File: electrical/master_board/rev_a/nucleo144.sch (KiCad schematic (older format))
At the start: 1 part, among them CN95 NUCLEO-F767ZI;2xF2x35

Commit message: Switched from x166 to x165 shift registers.  Add bin/spi_sim.py.
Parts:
- added Q25: 2N7000;SOT23, Package_TO_SOT_SMD:SOT-23, symbol Transistor_FET:2N7000
- added R68: 100KΩ;1608, Resistor_SMD:R_0603_1608Metric, symbol Device:R_US
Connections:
- net labels added: 3.3V, DIO_SS
- wire segments 108 -> 120
- no-connect marks 58 -> 56
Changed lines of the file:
@@
 Wire Wire Line
 	10000 4700 10000 4800
-Text HLabel 8100 5950 0    50   Input ~ 0
+Text HLabel 6700 6000 0    50   Input ~ 0
 GND
 Wire Wire Line
-	8100 5950 10000 5950
-Wire Wire Line
-	10000 5950 10000 5700
+	6700 6000 7100 6000
+Wire Wire Line
+	10000 6000 10000 5700
 Connection ~ 10000 5700
 NoConn ~ 8400 4800
@@
 Text HLabel 3500 2900 2    50   Output ~ 0
 RMOTOR_CTL2
-Text HLabel 7000 4700 2    50   Input ~ 0
+Text HLabel 4600 7200 2    50   Input ~ 0
 ~MOTOR_FAULT_IN
 Text HLabel 6000 2000 2    50   Input ~ 0
@@
 DIO_MISO
 Wire Wire Line
-	5500 3200 6000 3200
+	5500 3200 5700 3200
 Wire Wire Line
 	6000 3300 5500 3300
@@
 Wire Wire Line
 	6000 1000 5500 1000
-Text HLabel 7000 4800 2    50   Output ~ 0
+Text HLabel 4600 7300 2    50   Output ~ 0
 ~MOTOR_FAULT_OUT
 Wire Wire Line
-	7000 4700 6900 4700
-Wire Wire Line
-	6900 4700 6900 4800
-Wire Wire Line
-	6900 4800 7000 4800
+	4600 7200 4500 7200
+Wire Wire Line
+	4500 7200 4500 7300
+Wire Wire Line
+	4500 7300 4600 7300
 Wire Wire Line
 	5500 1400 6000 1400
-Text HLabel 7000 4500 2    50   Input ~ 0
+Text HLabel 4600 7000 2    50   Input ~ 0
 ~ESTOP_IN
 Text HLabel 6000 1500 2    50   Input ~ 0
@@
 Text Notes 8850 4350 0    50   ~ 0
 Morpho Power Pins.
-Text HLabel 7000 4600 2    50   Output ~ 0
+Text HLabel 4600 7100 2    50   Output ~ 0
 ~MOTOR_SLEEP
 Wire Wire Line
-	7000 4500 6900 4500
-Wire Wire Line
-	6900 4500 6900 4600
-Wire Wire Line
-	6900 4600 7000 4600
+	4600 7000 4500 7000
+Wire Wire Line
+	4500 7000 4500 7100
+Wire Wire Line
+	4500 7100 4600 7100
 Wire Wire Line
 	5500 1500 6000 1500
@@
 Wire Wire Line
 	5500 800  6000 800
-Text Notes 6900 4400 0    50   ~ 0
+Text Notes 4500 6900 0    50   ~ 0
 Cross Sheet Connetions
 Text HLabel 3500 5000 2    50   Input ~ 0
@@
 Text HLabel 6000 5600 2    50   Input ~ 0
 SERVO_POS
-NoConn ~ 7000 5000
-NoConn ~ 7000 5100
 Wire Wire Line
 	5500 1100 6000 1100
 Wire Wire Line
 	5500 5600 6000 5600
+$Comp
+L Transistor_FET:2N7000 Q?
+U 1 1 5FC61D2B
+P 7000 5400
+AR Path="/5F79BC00/5FC61D2B" Ref="Q?"  Part="1"
+AR Path="/5FA4A874/5FC61D2B" Ref="Q?"  Part="1"
+AR Path="/5FAD82EE/5FC61D2B" Ref="Q?"  Part="1"
+AR Path="/5F8C2F57/5FC61D2B" Ref="Q?"  Part="1"
+AR Path="/5F3221A2/5FC61D2B" Ref="Q25"  Part="1"
+F 0 "Q25" H 6900 5550 50  0000 L CNN
+F 1 "2N7000;SOT23" H 7150 5250 50  0000 L CNN
+F 2 "Package_TO_SOT_SMD:SOT-23" H 7200 5325 50  0001 L CIN
+F 3 "https://www.fairchildsemi.com/datasheets/2N/2N7000.pdf" H 7000 5400 50  0001 L CNN
+	1    7000 5400
+	1    0    0    -1
+$EndComp
+Wire Wire Line
+	5700 3200 5700 4400
+Wire Wire Line
+	5700 4400 6200 4400
+Wire Wire Line
+	6200 4400 6200 5400
+Wire Wire Line
+	6200 5400 6800 5400
+Connection ~ 5700 3200
+Wire Wire Line
+	5700 3200 6000 3200
+Connection ~ 7100 6000
+Wire Wire Line
+	7100 6000 10000 6000
+$Comp
+L Device:R_US R?
+U 1 1 5FC830FC
+P 7100 4850
+AR Path="/5F52F39E/5FC830FC" Ref="R?"  Part="1"
+AR Path="/5F3221A2/5FC830FC" Ref="R68"  Part="1"
+F 0 "R68" H 6950 4950 50  0000 L CNN
+F 1 "100KΩ;1608" H 7150 4750 50  0000 L CNN
+F 2 "Resistor_SMD:R_0603_1608Metric" V 7140 4840 50  0001 C CNN
+F 3 "~" H 7100 4850 50  0001 C CNN
+	1    7100 4850
+	1    0    0    -1
+$EndComp
+Wire Wire Line
+	7100 5200 7100 5100
+Wire Wire Line
+	7100 5600 7100 6000
+Text HLabel 6850 4600 0    50   Input ~ 0
+3.3V
+Wire Wire Line
+	6850 4600 7100 4600
+Wire Wire Line
+	7100 4600 7100 4700
+Text HLabel 7350 5100 2    50   Output ~ 0
+DIO_SS
+Wire Wire Line
+	7350 5100 7100 5100
+Connection ~ 7100 5100
+Wire Wire Line
+	7100 5100 7100 5000
 $EndSCHEMATC

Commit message: Change to sch and pcb
    Made following changes:
     - Remove Mikrobus connectors from sch and pcb
     - Change board to 4 layers
     - Add GND layer
     - Add 5V layer
     - Add 3.3V zone to 5V layer (experiment)
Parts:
- removed Q25: 2N7000;SOT23, Package_TO_SOT_SMD:SOT-23, symbol Transistor_FET:2N7000
- removed R68: 100KΩ;1608, Resistor_SMD:R_0603_1608Metric, symbol Device:R_US
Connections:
- net labels removed: 3.3V, DIO_SS
- wire segments 120 -> 108
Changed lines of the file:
@@
 $Descr A 11000 8500
 encoding utf-8
-Sheet 10 10
+Sheet 9 10
 Title "HR2 Nucleo"
 Date "2020-11-22"
@@
 Wire Wire Line
 	10000 4700 10000 4800
-Text HLabel 6700 6000 0    50   Input ~ 0
-GND
-Wire Wire Line
-	6700 6000 7100 6000
 Wire Wire Line
 	10000 6000 10000 5700
@@
 DIO_MISO
 Wire Wire Line
-	5500 3200 5700 3200
-Wire Wire Line
 	6000 3300 5500 3300
 Wire Wire Line
@@
 Wire Wire Line
 	5500 5600 6000 5600
-$Comp
-L Transistor_FET:2N7000 Q?
-U 1 1 5FC61D2B
-P 7000 5400
-AR Path="/5F79BC00/5FC61D2B" Ref="Q?"  Part="1"
-AR Path="/5FA4A874/5FC61D2B" Ref="Q?"  Part="1"
-AR Path="/5FAD82EE/5FC61D2B" Ref="Q?"  Part="1"
-AR Path="/5F8C2F57/5FC61D2B" Ref="Q?"  Part="1"
-AR Path="/5F3221A2/5FC61D2B" Ref="Q25"  Part="1"
-F 0 "Q25" H 6900 5550 50  0000 L CNN
-F 1 "2N7000;SOT23" H 7150 5250 50  0000 L CNN
-F 2 "Package_TO_SOT_SMD:SOT-23" H 7200 5325 50  0001 L CIN
-F 3 "https://www.fairchildsemi.com/datasheets/2N/2N7000.pdf" H 7000 5400 50  0001 L CNN
-	1    7000 5400
-	1    0    0    -1
-$EndComp
-Wire Wire Line
-	5700 3200 5700 4400
-Wire Wire Line
-	5700 4400 6200 4400
-Wire Wire Line
-	6200 4400 6200 5400
-Wire Wire Line
-	6200 5400 6800 5400
-Connection ~ 5700 3200
-Wire Wire Line
-	5700 3200 6000 3200
-Connection ~ 7100 6000
-Wire Wire Line
-	7100 6000 10000 6000
-$Comp
-L Device:R_US R?
-U 1 1 5FC830FC
-P 7100 4850
-AR Path="/5F52F39E/5FC830FC" Ref="R?"  Part="1"
-AR Path="/5F3221A2/5FC830FC" Ref="R68"  Part="1"
-F 0 "R68" H 6950 4950 50  0000 L CNN
-F 1 "100KΩ;1608" H 7150 4750 50  0000 L CNN
-F 2 "Resistor_SMD:R_0603_1608Metric" V 7140 4840 50  0001 C CNN
-F 3 "~" H 7100 4850 50  0001 C CNN
-	1    7100 4850
-	1    0    0    -1
-$EndComp
-Wire Wire Line
-	7100 5200 7100 5100
-Wire Wire Line
-	7100 5600 7100 6000
-Text HLabel 6850 4600 0    50   Input ~ 0
-3.3V
-Wire Wire Line
-	6850 4600 7100 4600
-Wire Wire Line
-	7100 4600 7100 4700
-Text HLabel 7350 5100 2    50   Output ~ 0
-DIO_SS
-Wire Wire Line
-	7350 5100 7100 5100
-Connection ~ 7100 5100
-Wire Wire Line
-	7100 5100 7100 5000
+Text HLabel 8100 6000 0    50   Input ~ 0
+GND
+Wire Wire Line
+	8100 6000 10000 6000
+Wire Wire Line
+	5500 3200 6000 3200
 $EndSCHEMATC

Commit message: Fixed the schematic DRC errors.
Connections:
- net labels removed: A0, A1, A4_SDA, A5_SCL, D0_RX, D10_PWM_NSS, D11_PWM_MOSI, D12_MISO, D13_SCK, D1_TX, INT0, INT1
- wire segments 108 -> 96
- no-connect marks 56 -> 66
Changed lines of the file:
@@
 Text HLabel 6000 3200 2    50   Output ~ 0
 ~DIO_NSS
-Text HLabel 3500 1100 2    50   Input ~ 0
-A0
-Text HLabel 6000 5800 2    50   BiDi ~ 0
-A5_SCL
-Text HLabel 9000 1700 2    50   Output ~ 0
-D0_RX
-Text HLabel 9000 2200 2    50   Input ~ 0
-D1_TX
-Text HLabel 6000 2200 2    50   Output ~ 0
-D10_PWM_NSS
-Text HLabel 3500 1500 2    50   Output ~ 0
-D11_PWM_MOSI
-Text HLabel 3500 1400 2    50   Input ~ 0
-D12_MISO
-Text HLabel 3500 1300 2    50   Output ~ 0
-D13_SCK
 Text HLabel 9000 3500 2    50   Output ~ 0
 ~NRST
-Text HLabel 6000 2800 2    50   Input ~ 0
-INT0
-Text HLabel 6000 900  2    50   Input ~ 0
-INT1
 Text HLabel 3500 2300 2    50   Output ~ 0
 ~LEDS_NSS
@@
 Wire Wire Line
 	5500 4300 6000 4300
-Wire Wire Line
-	5500 2800 6000 2800
 $Comp
 L HR2:NUCLEO-F767ZI;2xF2x35 CN95
@@
 	5500 3800 6000 3800
 Wire Wire Line
-	3000 1500 3500 1500
-Wire Wire Line
-	3000 1400 3500 1400
-Wire Wire Line
-	3000 1300 3500 1300
-Wire Wire Line
 	5500 2900 5700 2900
 Wire Wire Line
@@
 Wire Wire Line
 	3400 1200 3400 1600
-Wire Wire Line
-	3000 1100 3500 1100
 Wire Wire Line
 	3000 1200 3400 1200
@@
 	3000 3300 3500 3300
 Wire Wire Line
-	8500 2200 9000 2200
-Wire Wire Line
-	9000 1700 8500 1700
-Wire Wire Line
 	5500 1600 6000 1600
 Wire Wire Line
@@
 Wire Wire Line
 	5500 2100 6000 2100
-Wire Wire Line
-	6000 2200 5500 2200
 Wire Wire Line
 	5500 5800 5700 5800
@@
 Wire Wire Line
 	5700 4550 5700 5800
-Connection ~ 5700 5800
-Wire Wire Line
-	5700 5800 6000 5800
 Wire Wire Line
 	3400 1600 4200 1600
@@
 Wire Wire Line
 	3300 1700 4100 1700
-Wire Wire Line
-	5500 900  6000 900
 Wire Wire Line
 	6000 1000 5500 1000
@@
 	4100 1700 4100 4550
 Wire Wire Line
-	3100 5700 3500 5700
-Connection ~ 3100 5700
-Wire Wire Line
 	3100 5100 3100 5700
 Wire Wire Line
 	3000 5100 3100 5100
-Wire Wire Line
-	3000 4800 3500 4800
 Wire Wire Line
 	3000 5600 3500 5600
@@
 	1    0    0    -1
 $EndComp
-Text HLabel 3500 5700 2    50   BiDi ~ 0
-A4_SDA
-Text HLabel 3500 4800 2    50   Input ~ 0
-A1
 Text HLabel 3500 5800 2    50   Output ~ 0
 LEDS_SCLK
@@
 Wire Wire Line
 	5500 3200 6000 3200
+NoConn ~ 8500 2200
+NoConn ~ 8500 1700
+NoConn ~ 5500 2800
+NoConn ~ 5500 2200
+NoConn ~ 5500 900
+NoConn ~ 3000 1100
+NoConn ~ 3000 1300
+NoConn ~ 3000 1400
+NoConn ~ 3000 1500
+NoConn ~ 3000 4800
 $EndSCHEMATC

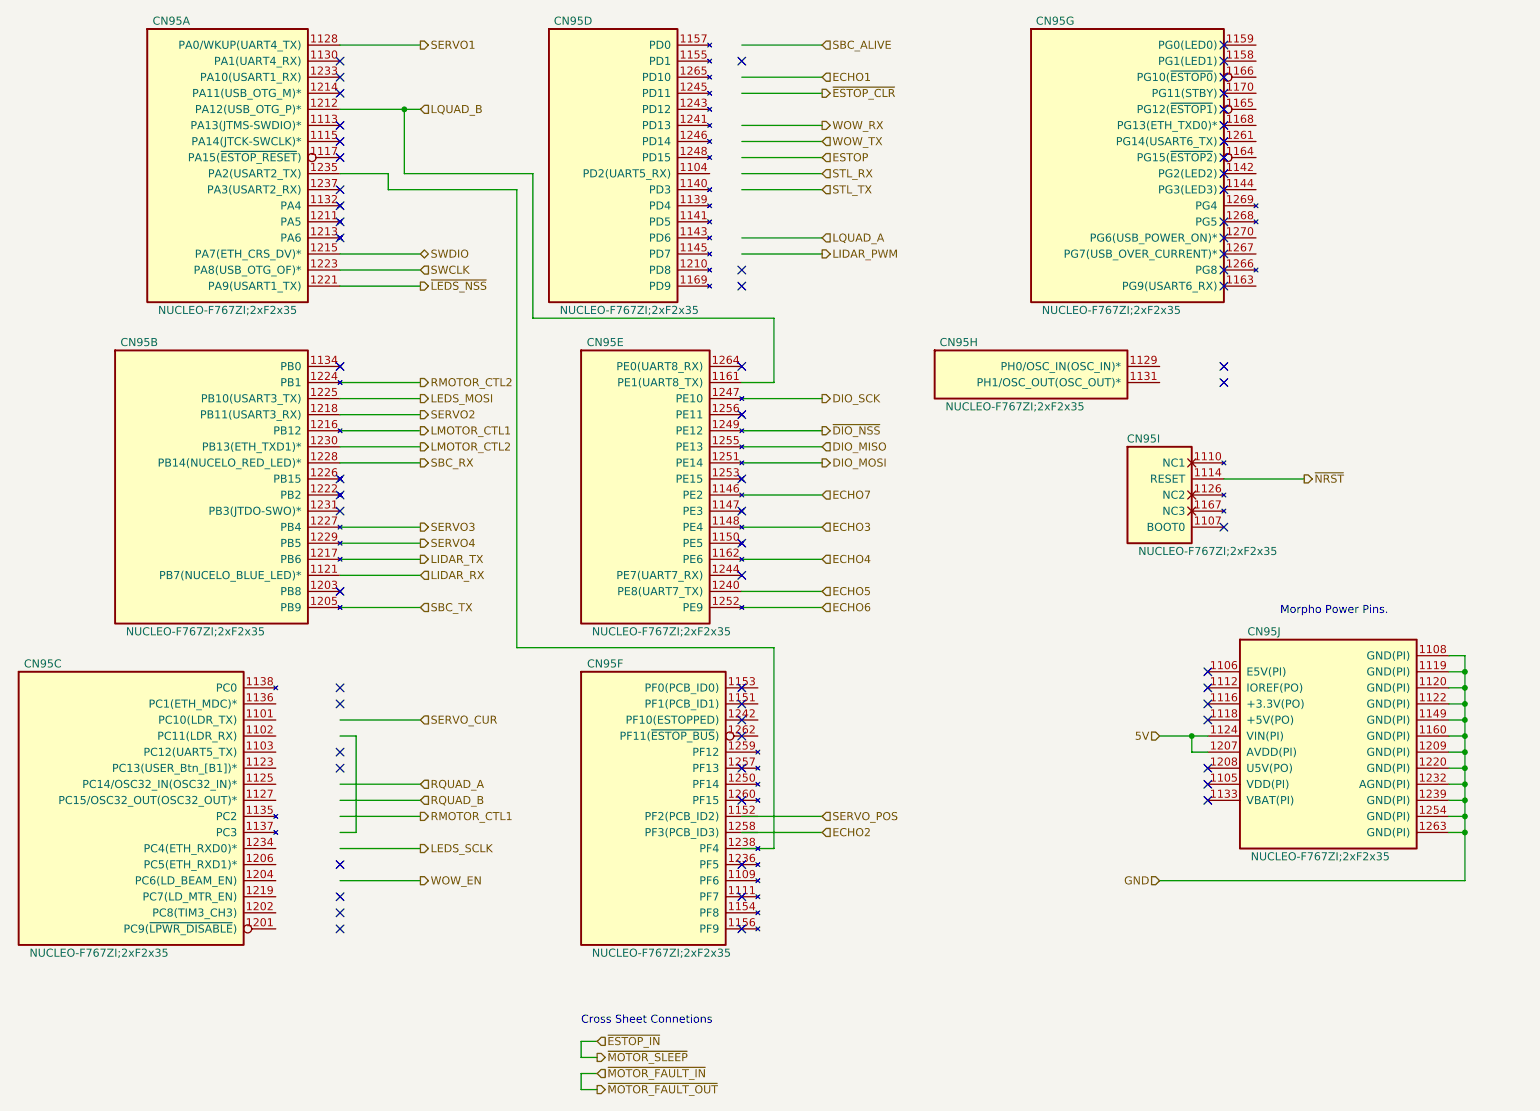
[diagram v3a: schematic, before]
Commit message: Updated WOWBus portion of schematic.
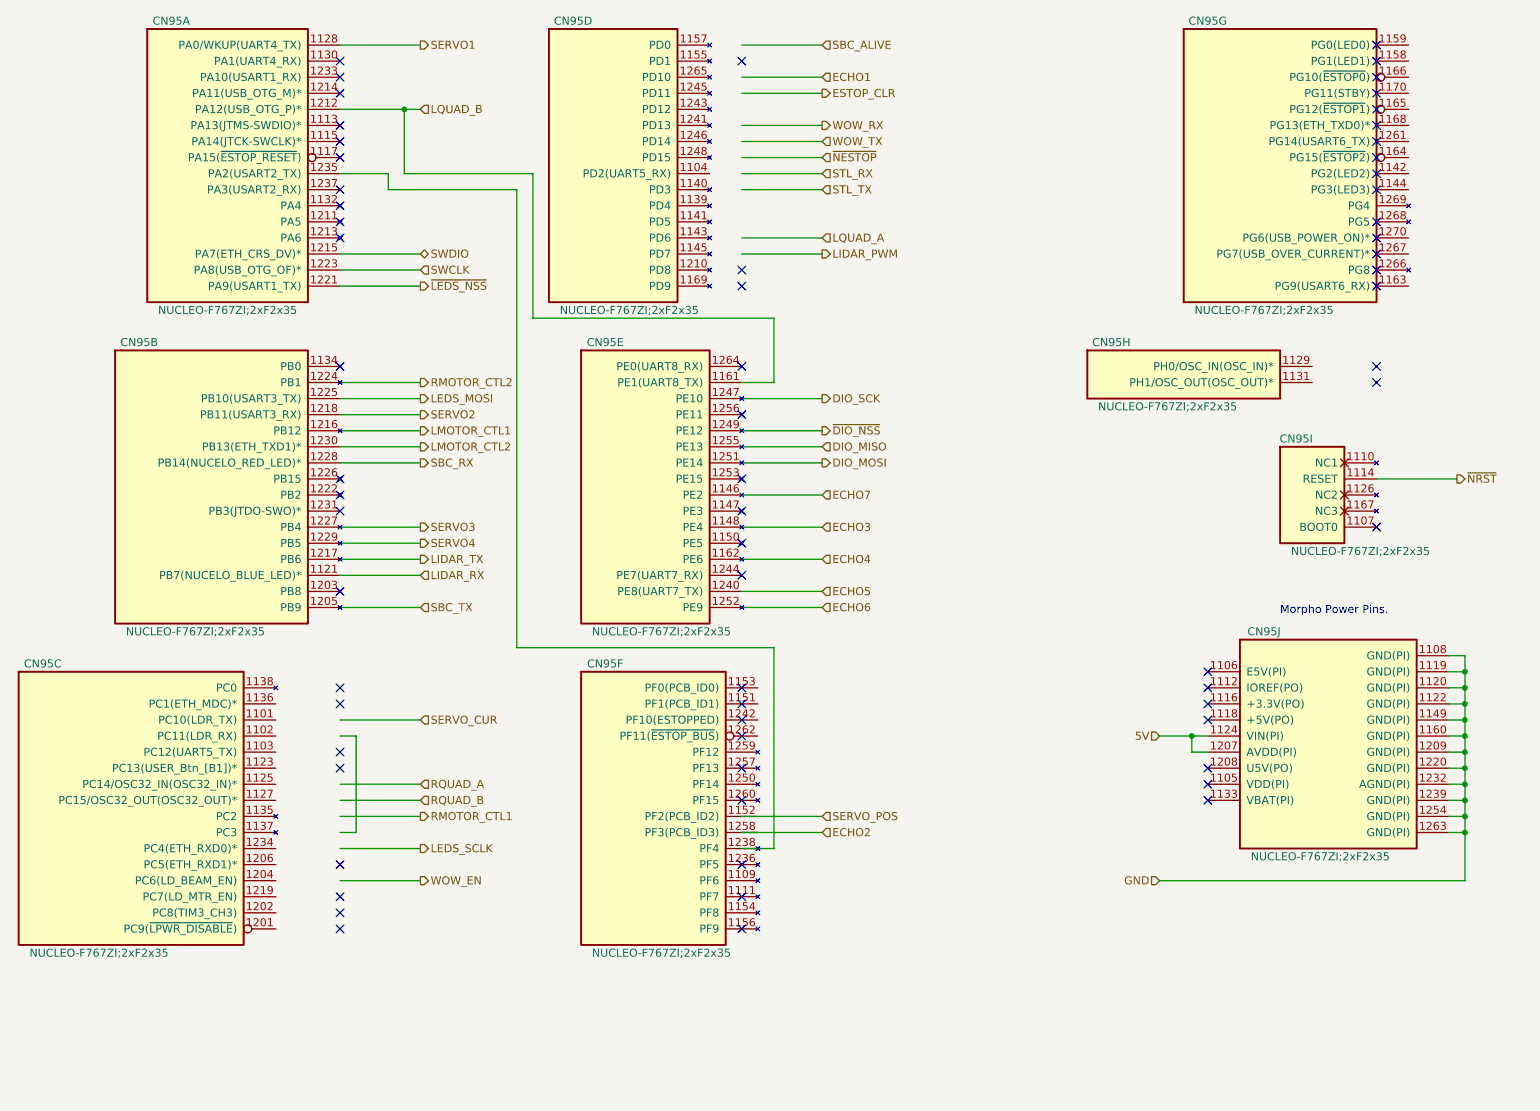
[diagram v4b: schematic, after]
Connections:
- net labels added: ESTOP_CLR, ~NESTOP
- net labels removed: ESTOP, ~ESTOP_CLR, ~ESTOP_IN, ~MOTOR_FAULT_IN, ~MOTOR_FAULT_OUT, ~MOTOR_SLEEP
- wire segments 96 -> 90
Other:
- note removed: "Cross Sheet Connetions"
- moved on the sheet: CN95G, CN95H, CN95I
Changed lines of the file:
@@
 $Descr A 11000 8500
 encoding utf-8
-Sheet 9 10
+Sheet 8 10
 Title "HR2 Nucleo"
 Date "2020-11-22"
@@
 L HR2:NUCLEO-F767ZI;2xF2x35 CN95
 U 7 1 5F352849
-P 7100 800
-F 0 "CN95" H 7450 950 50  0000 C CNN
-F 1 "NUCLEO-F767ZI;2xF2x35" H 7800 -850 50  0000 C CNN
-F 2 "HR2:NUCLEO_F767ZI_2xF2x35" H 7300 850 60  0001 L CNN
-F 3 "https://www.st.com/resource/en/user_manual/dm00244518-stm32-nucleo144-boards-stmicroelectronics.pdf" H 7300 650 60  0001 L CNN
-F 4 "https://www.st.com/resource/en/user_manual/dm00244518-stm32-nucleo144-boards-stmicroelectronics.pdf" H 7300 750 60  0001 L CNN "manf#"
-F 5 "NUCLEO144-F767ZI;Nucleo144 STM32F767ZI" H 7300 550 60  0001 L CNN "Field5"
-	7    7100 800
+P 8050 800
+F 0 "CN95" H 8400 950 50  0000 C CNN
+F 1 "NUCLEO-F767ZI;2xF2x35" H 8750 -850 50  0000 C CNN
+F 2 "HR2:NUCLEO_F767ZI_2xF2x35" H 8250 850 60  0001 L CNN
+F 3 "https://www.st.com/resource/en/user_manual/dm00244518-stm32-nucleo144-boards-stmicroelectronics.pdf" H 8250 650 60  0001 L CNN
+F 4 "https://www.st.com/resource/en/user_manual/dm00244518-stm32-nucleo144-boards-stmicroelectronics.pdf" H 8250 750 60  0001 L CNN "manf#"
+F 5 "NUCLEO144-F767ZI;Nucleo144 STM32F767ZI" H 8250 550 60  0001 L CNN "Field5"
+	7    8050 800
 	1    0    0    -1
 $EndComp
@@
 L HR2:NUCLEO-F767ZI;2xF2x35 CN95
 U 9 1 5F35A1BA
-P 7700 3400
-F 0 "CN95" H 8000 3550 50  0000 C CNN
-F 1 "NUCLEO-F767ZI;2xF2x35" H 8400 2850 50  0000 C CNN
-F 2 "HR2:NUCLEO_F767ZI_2xF2x35" H 7900 3450 60  0001 L CNN
-F 3 "https://www.st.com/resource/en/user_manual/dm00244518-stm32-nucleo144-boards-stmicroelectronics.pdf" H 7900 3250 60  0001 L CNN
-F 4 "https://www.st.com/resource/en/user_manual/dm00244518-stm32-nucleo144-boards-stmicroelectronics.pdf" H 7900 3350 60  0001 L CNN "manf#"
-F 5 "NUCLEO144-F767ZI;Nucleo144 STM32F767ZI" H 7900 3150 60  0001 L CNN "Field5"
-	9    7700 3400
+P 8650 3400
+F 0 "CN95" H 8950 3550 50  0000 C CNN
+F 1 "NUCLEO-F767ZI;2xF2x35" H 9350 2850 50  0000 C CNN
+F 2 "HR2:NUCLEO_F767ZI_2xF2x35" H 8850 3450 60  0001 L CNN
+F 3 "https://www.st.com/resource/en/user_manual/dm00244518-stm32-nucleo144-boards-stmicroelectronics.pdf" H 8850 3250 60  0001 L CNN
+F 4 "https://www.st.com/resource/en/user_manual/dm00244518-stm32-nucleo144-boards-stmicroelectronics.pdf" H 8850 3350 60  0001 L CNN "manf#"
+F 5 "NUCLEO144-F767ZI;Nucleo144 STM32F767ZI" H 8850 3150 60  0001 L CNN "Field5"
+	9    8650 3400
 	1    0    0    -1
 $EndComp
@@
 NoConn ~ 5500 5000
 NoConn ~ 5500 5100
-NoConn ~ 8500 3800
-NoConn ~ 8500 800
-NoConn ~ 8500 900
-NoConn ~ 8500 1000
-NoConn ~ 8500 1100
-NoConn ~ 8500 1200
-NoConn ~ 8500 1300
-NoConn ~ 8500 1400
-NoConn ~ 8500 1500
-NoConn ~ 8500 1600
-NoConn ~ 8500 2000
-NoConn ~ 8500 2100
-NoConn ~ 8500 2300
+NoConn ~ 9450 3800
+NoConn ~ 9450 800
+NoConn ~ 9450 900
+NoConn ~ 9450 1000
+NoConn ~ 9450 1100
+NoConn ~ 9450 1200
+NoConn ~ 9450 1300
+NoConn ~ 9450 1400
+NoConn ~ 9450 1500
+NoConn ~ 9450 1600
+NoConn ~ 9450 2000
+NoConn ~ 9450 2100
+NoConn ~ 9450 2300
 NoConn ~ 3000 900
 NoConn ~ 3000 1000
@@
 Text HLabel 3500 2900 2    50   Output ~ 0
 RMOTOR_CTL2
-Text HLabel 4600 7200 2    50   Input ~ 0
-~MOTOR_FAULT_IN
 Text HLabel 6000 2000 2    50   Input ~ 0
 LQUAD_A
@@
 NoConn ~ 5500 2300
 NoConn ~ 5500 3700
-NoConn ~ 8500 1900
+NoConn ~ 9450 1900
 NoConn ~ 5500 5300
 NoConn ~ 5500 5500
@@
 Text HLabel 6000 3200 2    50   Output ~ 0
 ~DIO_NSS
-Text HLabel 9000 3500 2    50   Output ~ 0
+Text HLabel 9950 3500 2    50   Output ~ 0
 ~NRST
 Text HLabel 3500 2300 2    50   Output ~ 0
@@
 	5500 5800 5700 5800
 Wire Wire Line
-	8500 3500 9000 3500
+	9450 3500 9950 3500
 Wire Wire Line
 	3500 4300 3000 4300
@@
 Wire Wire Line
 	5500 3000 6000 3000
-NoConn ~ 8500 2900
-NoConn ~ 8500 2800
+NoConn ~ 9450 2900
+NoConn ~ 9450 2800
 $Comp
 L HR2:NUCLEO-F767ZI;2xF2x35 CN95
 U 8 1 5F355CEA
-P 6500 2800
-F 0 "CN95" H 6850 2950 50  0000 C CNN
-F 1 "NUCLEO-F767ZI;2xF2x35" H 7200 2550 50  0000 C CNN
-F 2 "HR2:NUCLEO_F767ZI_2xF2x35" H 6700 2850 60  0001 L CNN
-F 3 "https://www.st.com/resource/en/user_manual/dm00244518-stm32-nucleo144-boards-stmicroelectronics.pdf" H 6700 2650 60  0001 L CNN
-F 4 "https://www.st.com/resource/en/user_manual/dm00244518-stm32-nucleo144-boards-stmicroelectronics.pdf" H 6700 2750 60  0001 L CNN "manf#"
-F 5 "NUCLEO144-F767ZI;Nucleo144 STM32F767ZI" H 6700 2550 60  0001 L CNN "Field5"
-	8    6500 2800
+P 7450 2800
+F 0 "CN95" H 7800 2950 50  0000 C CNN
+F 1 "NUCLEO-F767ZI;2xF2x35" H 8150 2550 50  0000 C CNN
+F 2 "HR2:NUCLEO_F767ZI_2xF2x35" H 7650 2850 60  0001 L CNN
+F 3 "https://www.st.com/resource/en/user_manual/dm00244518-stm32-nucleo144-boards-stmicroelectronics.pdf" H 7650 2650 60  0001 L CNN
+F 4 "https://www.st.com/resource/en/user_manual/dm00244518-stm32-nucleo144-boards-stmicroelectronics.pdf" H 7650 2750 60  0001 L CNN "manf#"
+F 5 "NUCLEO144-F767ZI;Nucleo144 STM32F767ZI" H 7650 2550 60  0001 L CNN "Field5"
+	8    7450 2800
 	1    0    0    -1
 $EndComp
@@
 Wire Wire Line
 	6000 1000 5500 1000
-Text HLabel 4600 7300 2    50   Output ~ 0
-~MOTOR_FAULT_OUT
-Wire Wire Line
-	4600 7200 4500 7200
-Wire Wire Line
-	4500 7200 4500 7300
-Wire Wire Line
-	4500 7300 4600 7300
 Wire Wire Line
 	5500 1400 6000 1400
-Text HLabel 4600 7000 2    50   Input ~ 0
-~ESTOP_IN
 Text HLabel 6000 1500 2    50   Input ~ 0
-ESTOP
+~NESTOP
 Text Notes 8850 4350 0    50   ~ 0
 Morpho Power Pins.
-Text HLabel 4600 7100 2    50   Output ~ 0
-~MOTOR_SLEEP
-Wire Wire Line
-	4600 7000 4500 7000
-Wire Wire Line
-	4500 7000 4500 7100
-Wire Wire Line
-	4500 7100 4600 7100
-Wire Wire Line
-	5500 1500 6000 1500
 Wire Wire Line
 	4100 1700 4100 4550
@@
 NoConn ~ 3000 4900
 Text HLabel 6000 1100 2    50   Output ~ 0
-~ESTOP_CLR
+ESTOP_CLR
 Wire Wire Line
 	3000 5000 3500 5000
@@
 Wire Wire Line
 	5500 800  6000 800
-Text Notes 4500 6900 0    50   ~ 0
-Cross Sheet Connetions
 Text HLabel 3500 5000 2    50   Input ~ 0
 SERVO_CUR
@@
 Wire Wire Line
 	5500 3200 6000 3200
-NoConn ~ 8500 2200
-NoConn ~ 8500 1700
+NoConn ~ 9450 2200
+NoConn ~ 9450 1700
 NoConn ~ 5500 2800
 NoConn ~ 5500 2200
@@
 NoConn ~ 3000 1500
 NoConn ~ 3000 4800
+Wire Wire Line
+	5500 1500 6000 1500
 $EndSCHEMATC
